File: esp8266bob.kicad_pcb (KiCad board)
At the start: 2 copper layers, 50 x 50 mm, 46 parts, among them P1 USB_OTG, P2 CONN_01X07, P3 CONN_01X07, P4 CONN_01X03, U1 TS 2940 CP33, U10 WS2812, U11 WS2812, U12 WS2812, U2 ESP-07v2, U3 WS2812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

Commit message: PCB!!!
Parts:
- added FID1: Fiducial_1mm_Dia_2.54mm_Outer_CopperTop, Fiducials:Fiducial_1mm_Dia_2.54mm_Outer_CopperTop, F.Cu at (221.0, 58.4)
- added FID2: Fiducial_1mm_Dia_2.54mm_Outer_CopperTop, Fiducials:Fiducial_1mm_Dia_2.54mm_Outer_CopperTop, F.Cu at (221.0, 101.6)
- added FID3: Fiducial_1mm_Dia_2.54mm_Outer_CopperTop, Fiducials:Fiducial_1mm_Dia_2.54mm_Outer_CopperTop, F.Cu at (264.2, 101.6)
- JP1, JP2: moved to B.Cu
- moved C3 32.6 mm to (222.5, 78.5), turned to 180 degrees
- moved C4 29.2 mm to (222.5, 77.0), turned to 180 degrees
- moved U1 22.8 mm to (229.1, 83.1), turned to 90 degrees
- moved U9 22.2 mm to (229.2, 72.7), turned to 0 degrees
- moved C20 21.8 mm to (250.1, 77.5), turned to 180 degrees
- moved C7 19.9 mm to (235.7, 73.2), turned to 270 degrees
- moved P4 19.8 mm to (221.0, 68.6), turned to 0 degrees
- moved C10 16.6 mm to (234.4, 100.3), turned to 270 degrees
- moved Y1 14.2 mm to (235.7, 81.0)
- moved P1 13.7 mm to (222.2, 92.7), turned to 270 degrees
- moved C1 13.7 mm to (227.6, 87.6)
- moved C2 13.4 mm to (227.5, 89.3), turned to 180 degrees
- moved R3 12.6 mm to (235.7, 64.3)
- moved D1 11.4 mm to (231.5, 94.7)
- moved R2 11.3 mm to (240.7, 82.7)
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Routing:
- net GND: track 127.8 -> 308.2 mm, vias 2 -> 54
- net (no net): track 106.0 -> 0.00 mm
- net /CH340_RX: track 0.00 -> 38.5 mm, vias 0 -> 1
- net /CH340_TX: track 0.00 -> 33.9 mm, vias 0 -> 1
- net /Prog_pin: track 19.7 -> 52.8 mm, vias 0 -> 2
- net +5V: track 142.8 -> 170.3 mm, vias 0 -> 2
- net Net-(U10-Pad1): track 0.00 -> 27.4 mm, vias 0 -> 2
- net +3V3: track 41.4 -> 68.4 mm, vias 0 -> 2
- net Net-(U11-Pad1): track 0.00 -> 26.4 mm, vias 0 -> 2
- net /USB_D+: track 12.5 -> 26.6 mm
- net /USB_D-: track 14.0 -> 26.6 mm
- net /GPIO14: track 11.9 -> 24.4 mm, vias 0 -> 1
- net Net-(U3-Pad1): track 0.00 -> 12.3 mm, vias 0 -> 2
- net Net-(U10-Pad2): track 0.00 -> 11.7 mm, vias 0 -> 2
- net Net-(U4-Pad1): track 0.00 -> 11.4 mm, vias 0 -> 2
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- added copper zone on B.Cu, net GND
- added copper zone on F.Cu, net GND
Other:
- net class Default: trace_width 0.1524 -> 0.2
- net class Power added: clearance 0.2, trace_width 0.5, via_dia 1, via_drill 0.6
- rule trace_min: 0.1524 -> 0.2
- rule via_min_size: 0.4 -> 0.6

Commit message: gerber generated
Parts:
- added C18: 100n, Capacitors_SMD:C_0603_HandSoldering, F.Cu at (229.5, 60.8)
- added P5: CONN_01X03, Pin_Headers:Pin_Header_Straight_1x03, F.Cu at (265.3, 92.7)
- JP1: value RX -> JUMPER
- JP2: value TX -> JUMPER
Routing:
- net Net-(P5-Pad2): track 0.00 -> 12.5 mm
- net /RESET: track 19.9 -> 26.3 mm
- net GND: track 308.2 -> 313.9 mm
- net +5V: track 170.3 -> 174.8 mm

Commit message: finalize
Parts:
- added REF**: Symbol_OSHW-Logo_SilkScreen, Symbols:Symbol_OSHW-Logo_SilkScreen, F.Cu at (228.2, 99.4)
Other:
- board text added: "3v3"
- board text added: "5v"
- board text added: "ADC"
- board text added: "P0"
- board text added: "P12"
- board text added: "P13"
- board text added: "P14"
- board text added: "P16"
- board text added: "P4"
- board text added: "P5"
- board text added: "Pd"
- board text added: "Prg"
- board text added: "Rst"
- board text added: "Rx"
- board text added: "Tx"

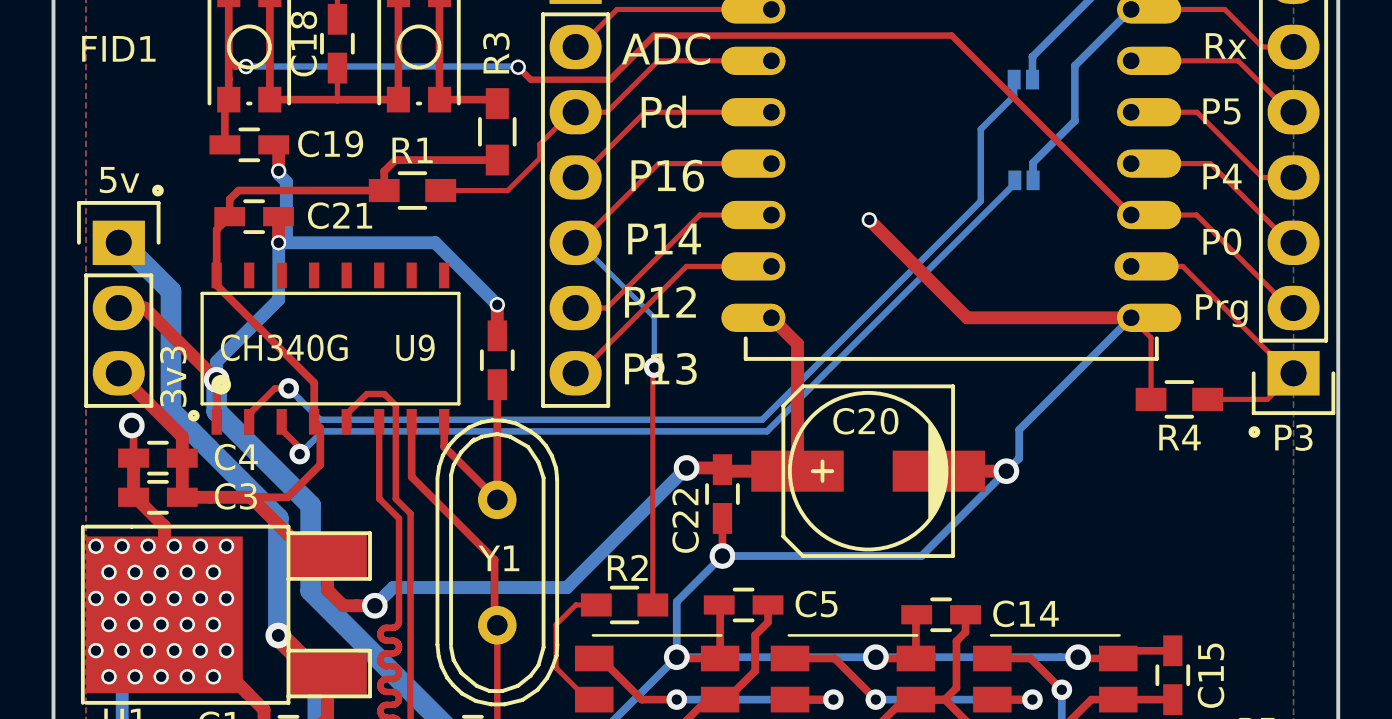
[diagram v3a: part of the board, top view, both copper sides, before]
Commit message: bugs fixed in the schematic
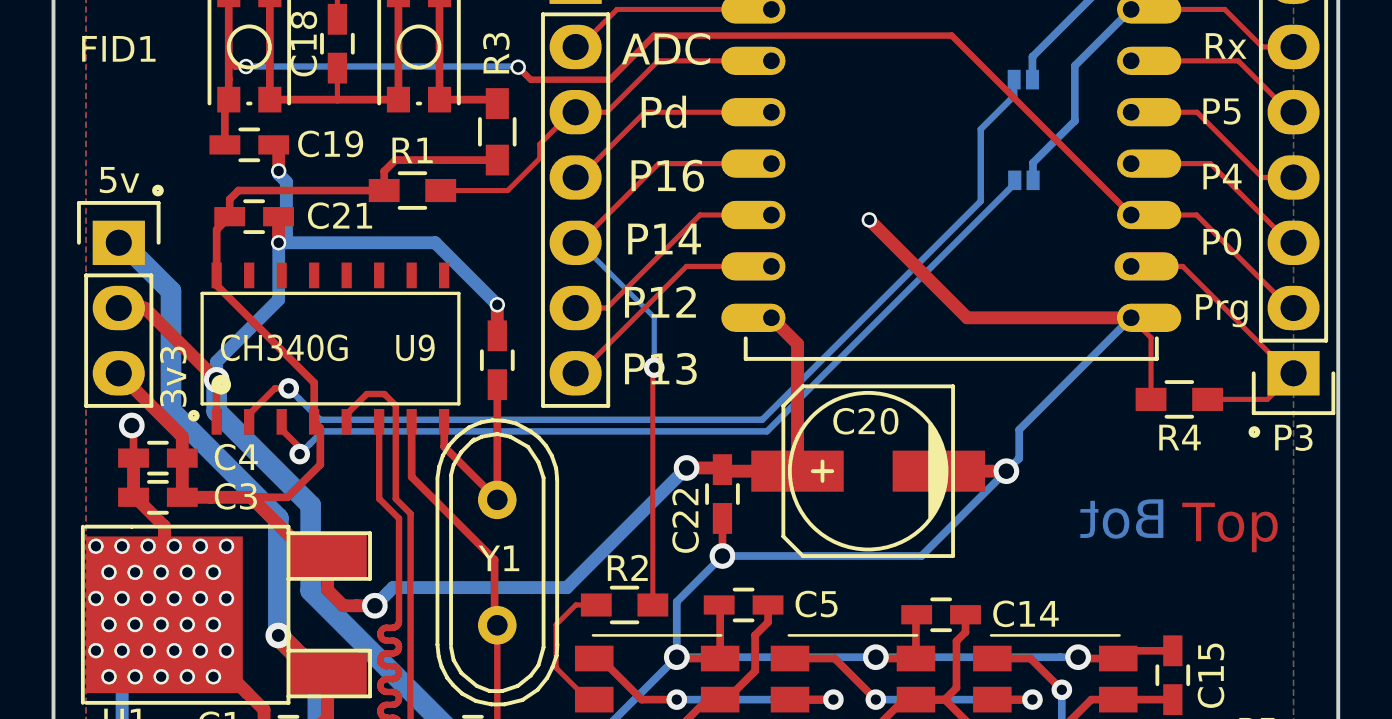
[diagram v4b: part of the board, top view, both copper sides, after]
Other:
- rule pad_to_mask_clearance: 0.2 -> 0
- board text added: "Bot"
- board text added: "Top"
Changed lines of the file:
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@@
 (kicad_pcb (version 4) (host pcbnew 4.0.2-4+6225~38~ubuntu15.10.1-stable)
   (general
-    (links 0)
+    (links 134)
     (no_connects 0)
-    (area 203.966904 50.624999 281.173096 105.955001)
+    (area 203.966904 50.624999 281.173096 106.97682)
     (thickness 1.6)
-    (drawings 24)
+    (drawings 26)
     (tracks 740)
     (zones 0)
@@
   )
   (setup
-    (last_trace_width 0.3)
+    (last_trace_width 0.2)
     (user_trace_width 0.1524)
     (user_trace_width 0.2)
@@
     (pad_size 1.524 1.524)
     (pad_drill 0.762)
-    (pad_to_mask_clearance 0.2)
+    (pad_to_mask_clearance 0)
     (solder_mask_min_width 0.0889)
     (aux_axis_origin 218.44 55.88)
@@
     (pcbplotparams
       (layerselection 0x010f8_80000001)
-      (usegerberextensions false)
+      (usegerberextensions true)
       (excludeedgelayer true)
       (linewidth 0.100000)
@@
       (drillshape 0)
       (scaleselection 1)
-      (outputdirectory ""))
+      (outputdirectory /home/luggi/kicad/boardfilesesp07/))
   )
   (net 0 "")
@@
     (fp_line (start 0.35052 0.89916) (end 0.7493 1.89992) (layer F.SilkS) (width 0.15))
   )
-  (gr_text 5v (at 220.98 66.167 360) (layer F.SilkS)
+  (gr_text Bot (at 260.096 79.375) (layer B.Cu)
+    (effects (font (size 1.5 1.5) (thickness 0.3)) (justify mirror))
+  )
+  (gr_text Top (at 264.287 79.502) (layer F.Cu)
+    (effects (font (size 1.5 1.5) (thickness 0.3)))
+  )
+  (gr_text 5v (at 220.98 66.167) (layer F.SilkS)
     (effects (font (size 1 1) (thickness 0.2)))
   )

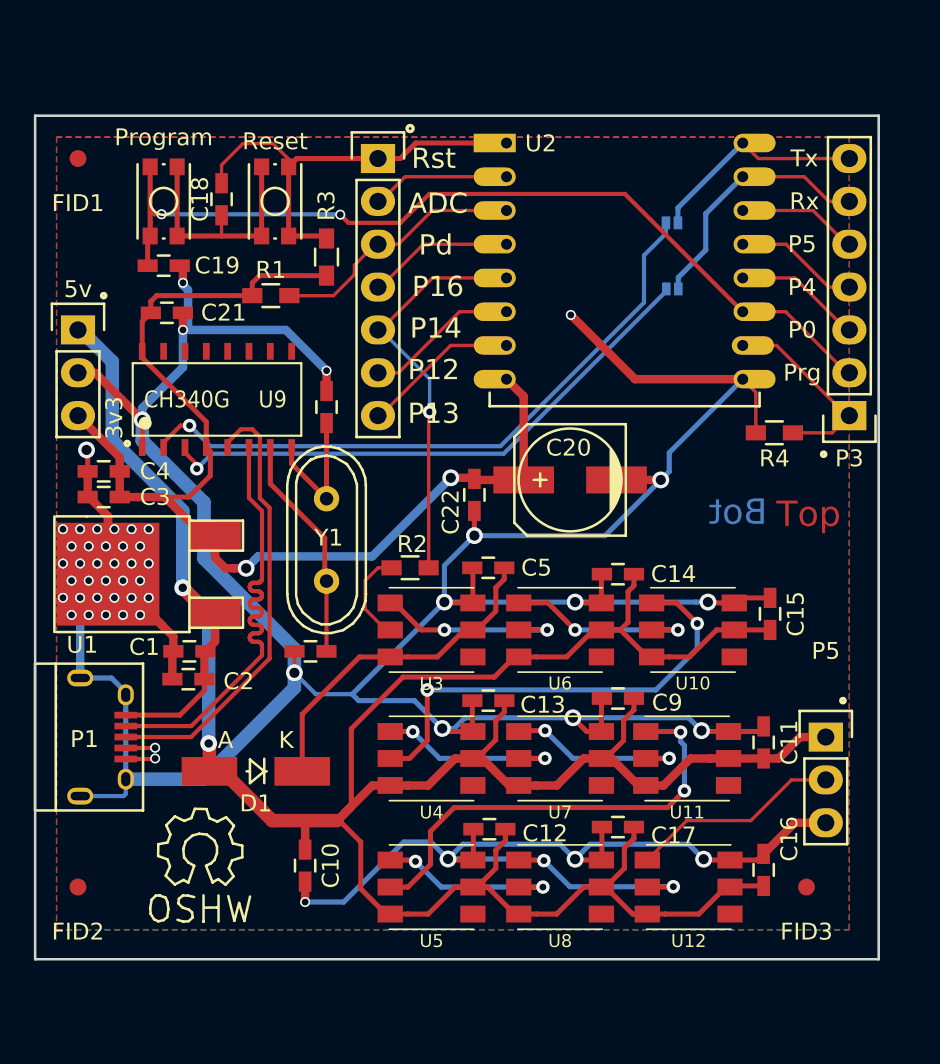
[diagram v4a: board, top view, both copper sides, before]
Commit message: bugfixes, auto programming pins connected
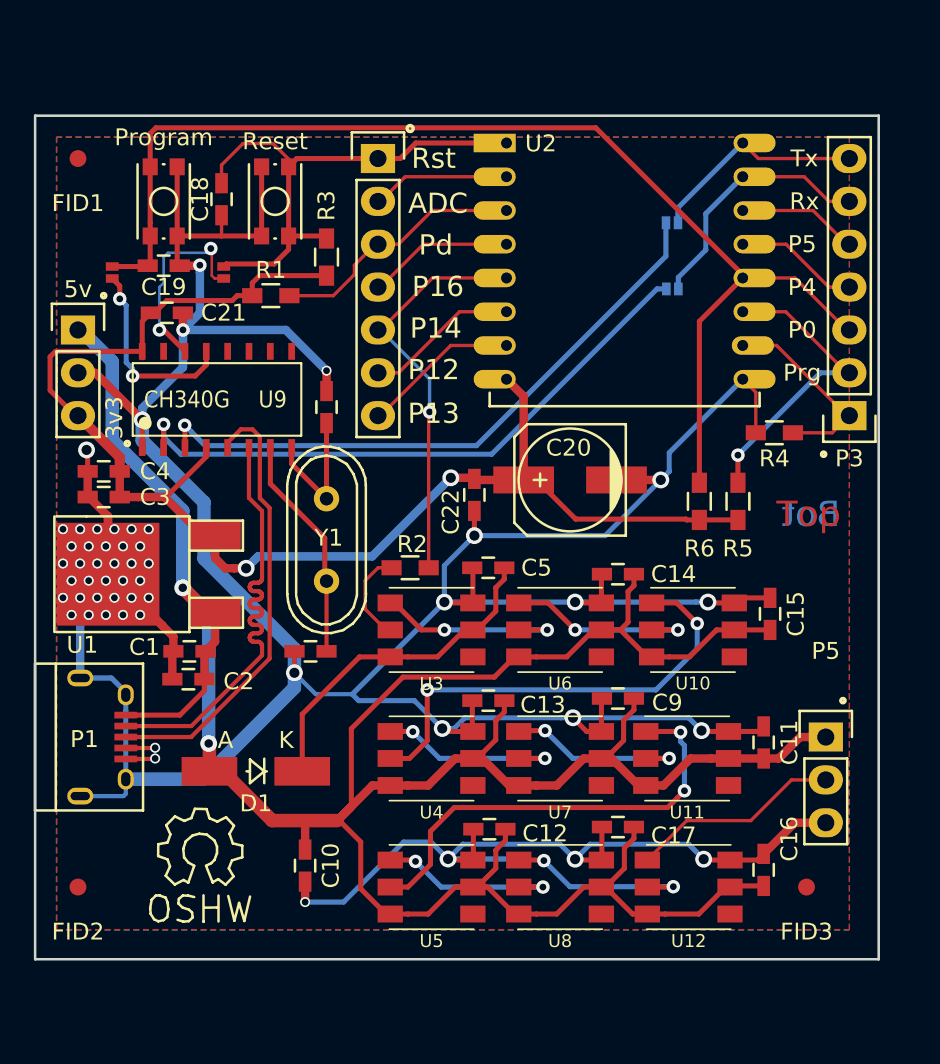
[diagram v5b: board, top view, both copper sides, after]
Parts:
- added JP3: JUMPER, open-project:S_JUMPER_2, F.Cu at (229.6, 65.2)
- added JP4: JUMPER, open-project:S_JUMPER_2, F.Cu at (223.0, 65.2)
- added R5: 10k, Resistors_SMD:R_0603_HandSoldering, F.Cu at (260.1, 78.7)
- added R6: 10k, Resistors_SMD:R_0603_HandSoldering, F.Cu at (257.8, 78.7)
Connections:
- C19 pad 1: /Prog_pin -> /GPIO0
- P3 pad 2: /Prog_pin -> /GPIO2
- Program pad 1: /Prog_pin -> /GPIO0
- U2 pad 11: /Prog_pin -> /GPIO2
- U9 pad 13: Net-(U9-Pad13) -> /DTR
- U9 pad 14: Net-(U9-Pad14) -> /RTS
- U9 pad 2: /CH340_RX -> /CH340_TX
- U9 pad 3: /CH340_TX -> /CH340_RX
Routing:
- net /GPIO0: track 7.60 -> 69.9 mm
- net /Prog_pin: track 52.7 -> 0.00 mm, vias 2 -> 0
- net /GPIO2: track 0.00 -> 18.1 mm, vias 0 -> 1
- net +3V3: track 68.3 -> 83.6 mm
- net /RTS: track 0.00 -> 11.9 mm, vias 0 -> 2
- net /DTR: track 0.00 -> 11.7 mm, vias 0 -> 2
- net GND: track 313.9 -> 305.3 mm, vias 54 -> 53
- net /RESET: track 26.3 -> 31.4 mm
- net /CH340_TX: track 33.9 -> 36.8 mm
- net /CH340_RX: track 38.5 -> 37.3 mm
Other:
- net class Default: clearance 0.2 -> 0.15; trace_width 0.2 -> 0.15
- rule trace_clearance: 0.2 -> 0.15
- rule trace_min: 0.2 -> 0.15
